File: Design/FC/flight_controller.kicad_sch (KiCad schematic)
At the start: 29 parts, among them U1 STM32H747BIT6, U3 BMI323, U4 MMC5983MA, U5 BMP390

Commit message: added flash memory
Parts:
- added C49: 100nF, symbol Device:C
- added FLASH_1: W25N01GWZEIG, Lib:W25N01GWZEIG, symbol W25N01GWZEIG:W25N01GWZEIG
- added R13, R14: 10K, symbol Device:R
- U1: footprint LQFP-208 -> Lib:STM32H747BIT6-LQFP-208
- U3: footprint BMI323_BOS -> Lib:BMI323_BOS
- U4: footprint MMC5983MA_MEM -> Lib:MMC5983MA_MEM
- U5: footprint BMP390-10LGA_2X2X0p75_BOS -> Lib:BMP390-10LGA_2X2X0p75_BOS
- renumbered BN880_Con to BN880_Con1, Debug_Con to Debug_Con1, Debug_UART to Debug_UART1, L_Motor to L_Motor1, RF_RECV_CONN to RF_RECV_CONN1, R_Motor to R_Motor1
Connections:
- net +3.3V: now also C49.1, FLASH_1.8 (VCC), R13.2, R14.1
- net GND: now also L_Servo_4.1 (Pin_1), U5.3 (VSS), C49.2, FLASH_1.4 (GND), FLASH_1.9 (EP)
- net FLASH_1_NSS: now reaches U1.166 (PA15)
- net FLASH_1_NSS: now also FLASH_1.1 (~{CS})
- net FLASH_1_SCK: now reaches U1.167 (PC10)
- net FLASH_1_SCK: now also FLASH_1.6 (CLK)
- net FLASH_1_MISO: now reaches U1.168 (PC11)
- net FLASH_1_MISO: now also FLASH_1.5 (DI_(IO0_))
- net FLASH_1_MOSI: now reaches U1.169 (PC12)
- net FLASH_1_MOSI: now also FLASH_1.2 (DO_(IO1_))
- net EXT_DEV_INT_BARO: no longer names the net of U1.66 (PI15)
- net I2C_1_SCL renamed CURRENT_SENSE_SCL
- net I2C_1_SDA renamed CURRENT_SENSE_SDA
- net TIM_4_CH_1: no longer names the net of U1.111 (PD12)
- new net: FLASH_1.3 (~{WP_(IO2_)}), R14.2
- new net: FLASH_1.7 (~{HOLD_(IO3_)}), R13.1
- no-connect marks 3 -> 111
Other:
- note added: "Current Sensor (Address: 0x40)"
- note added: "Flash Memory (1 Gbit)"
- moved on the sheet: C47, C48, RF_RECV_CONN1, U5

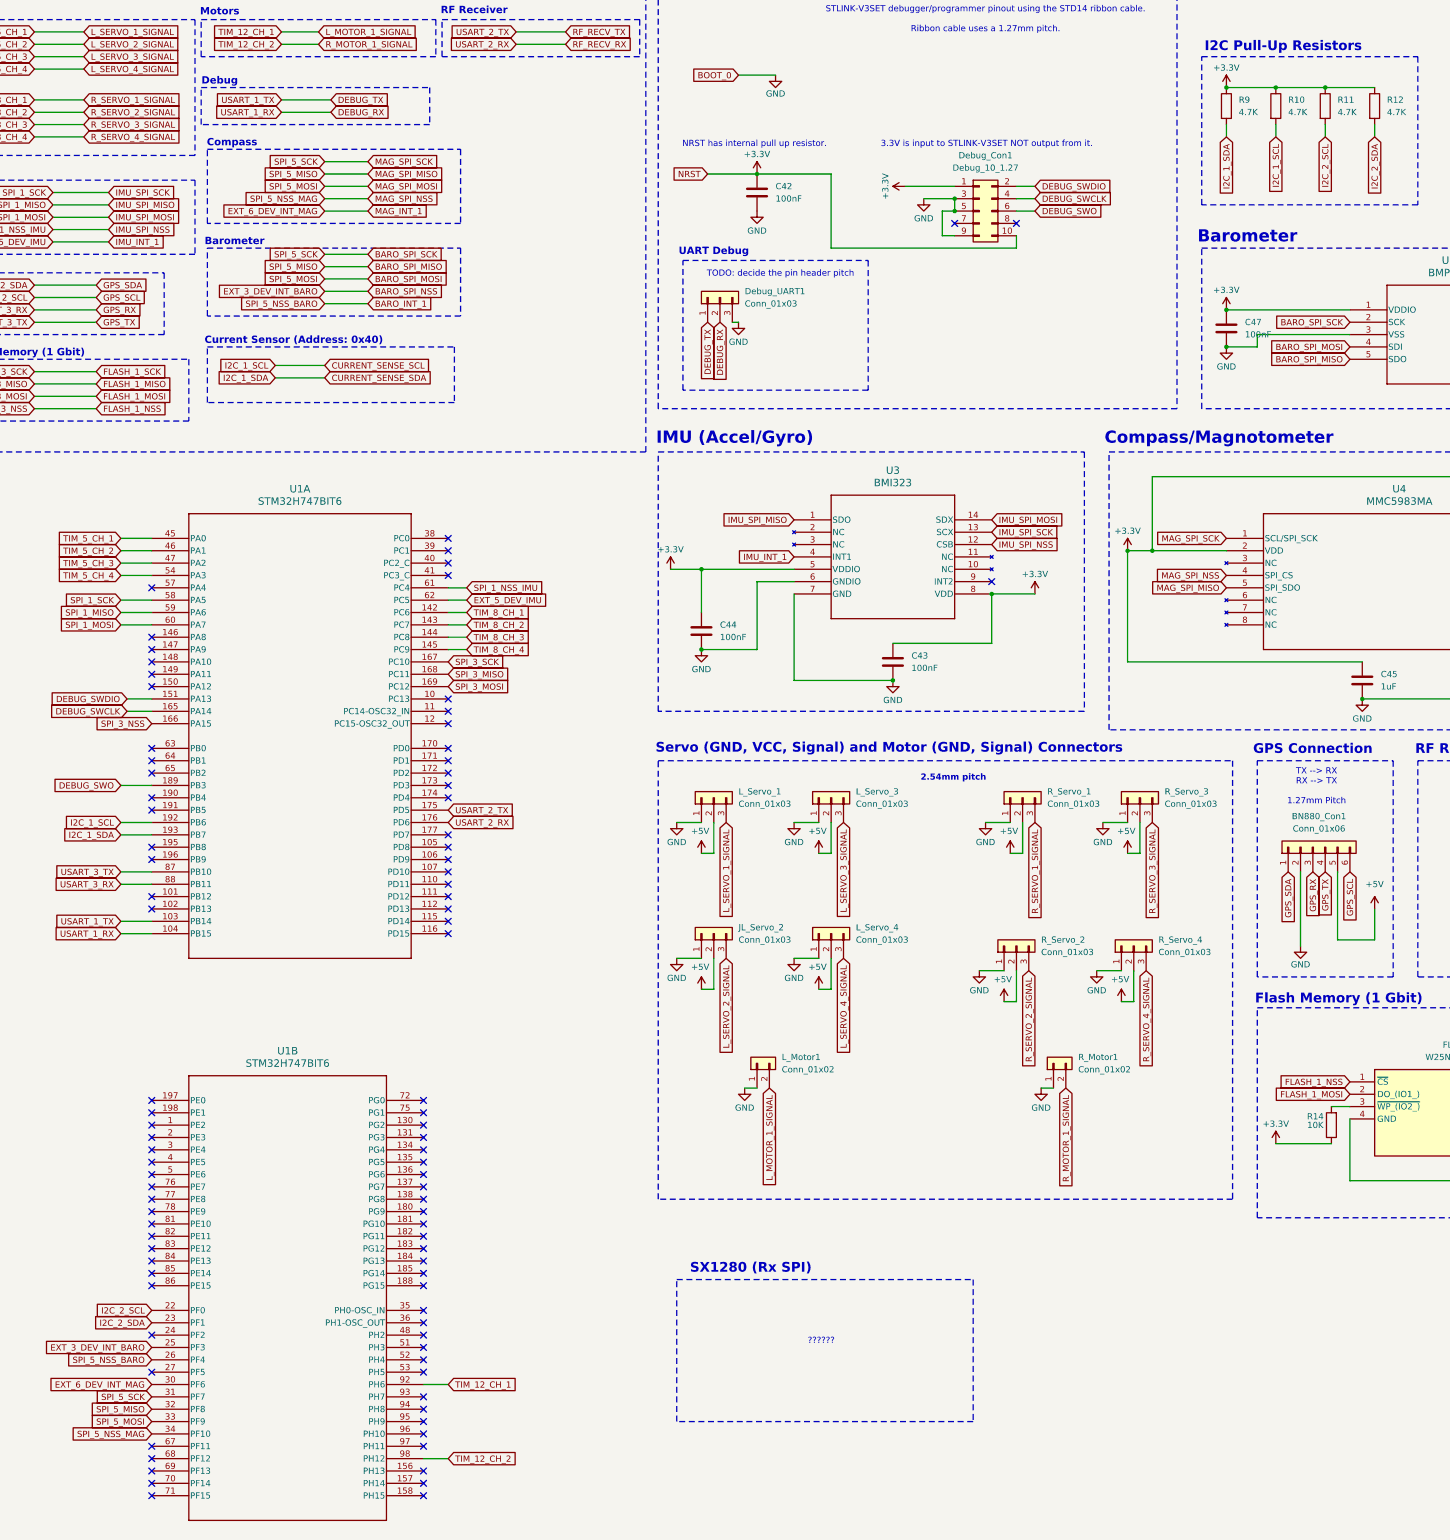
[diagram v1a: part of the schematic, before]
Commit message: started adding footprints and filling out bom
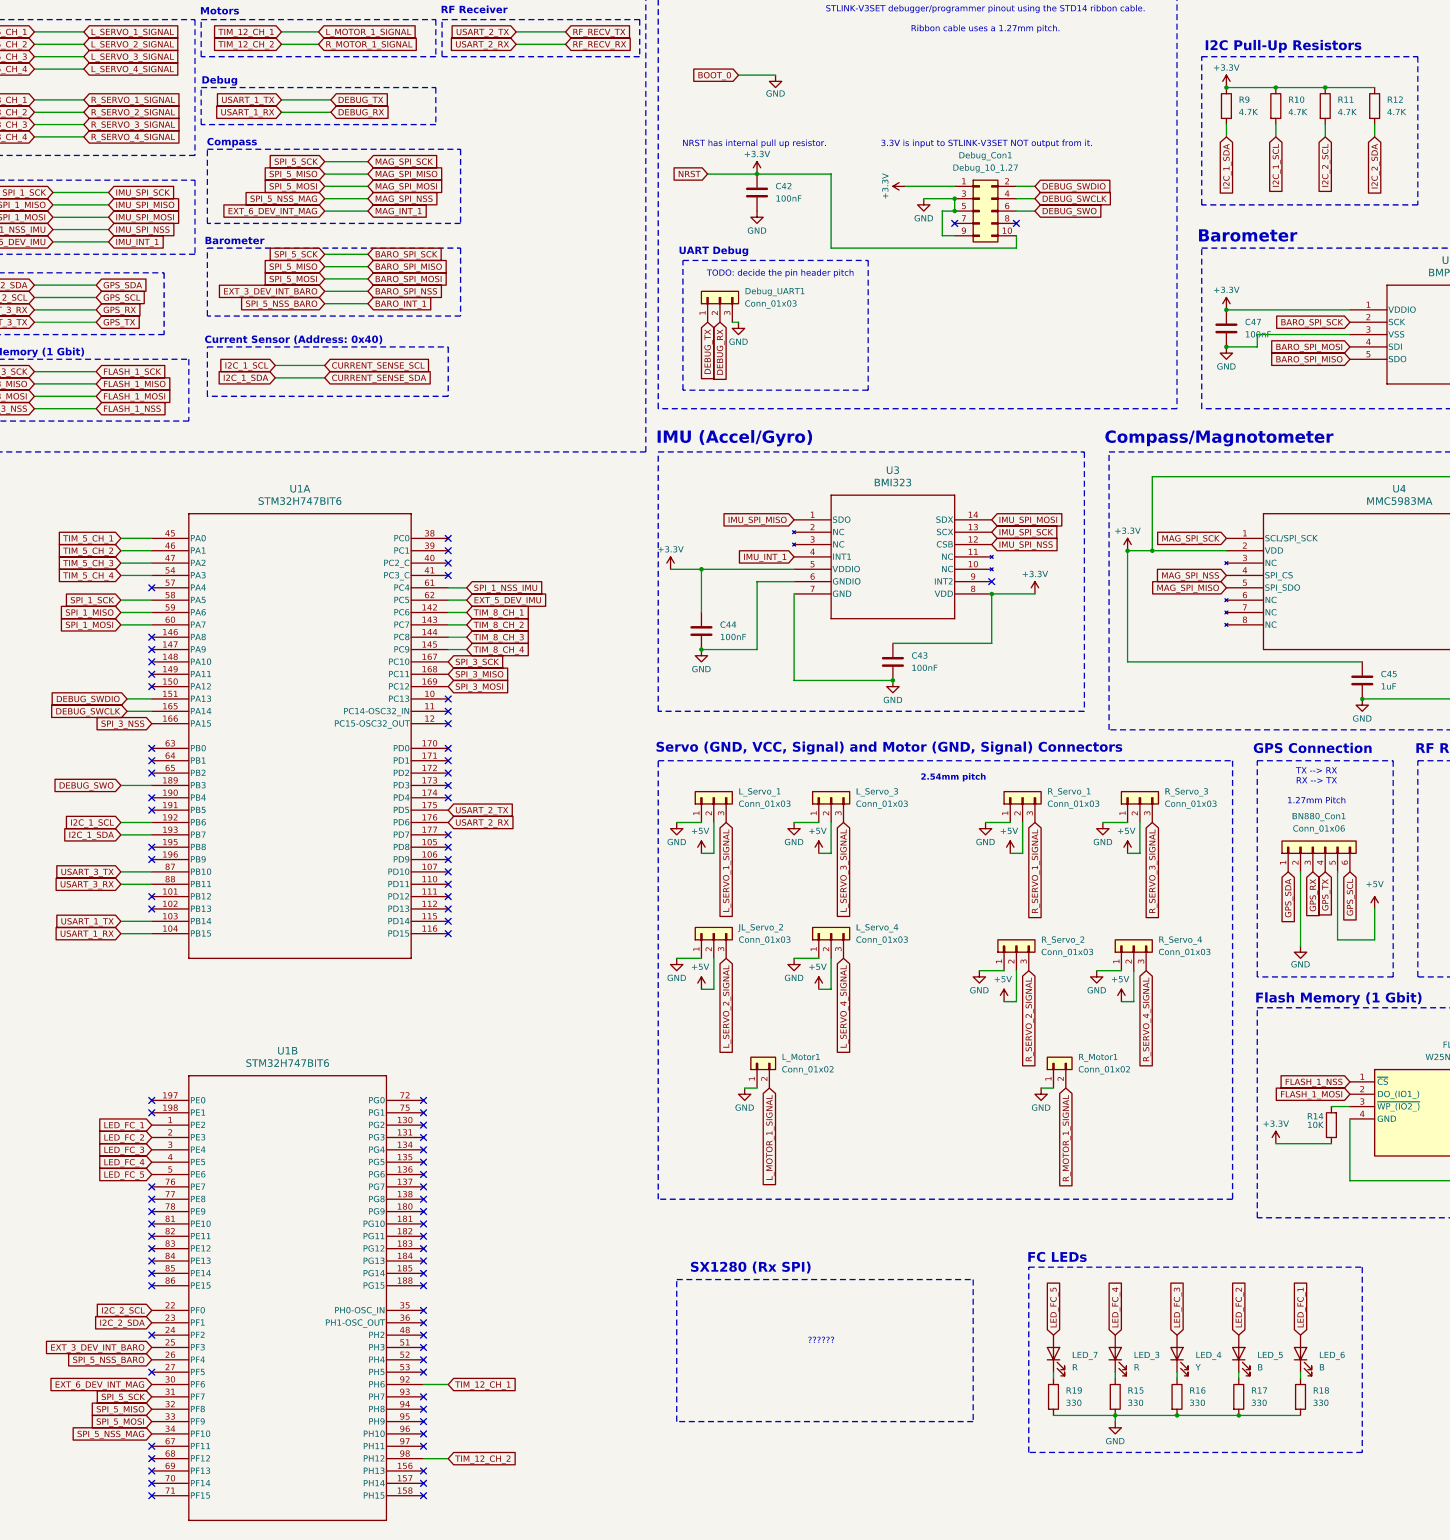
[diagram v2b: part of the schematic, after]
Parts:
- added LED_3, LED_7: R, symbol Device:LED
- added LED_4: Y, symbol Device:LED
- added LED_5, LED_6: B, symbol Device:LED
- added R15, R16, R17, R18, R19: 330, Resistor_SMD:R_0603_1608Metric_Pad0.98x0.95mm_HandSolder, symbol Device:R
- C42, C43, C44, C45, C46, C47, C48, C49: footprint (none) -> Capacitor_SMD:C_0603_1608Metric_Pad1.08x0.95mm_HandSolder
- Debug_Con1: footprint (none) -> Connector_PinHeader_1.27mm:PinHeader_2x05_P1.27mm_Vertical
- Debug_UART1, JL_Servo_2, L_Servo_1, L_Servo_3, L_Servo_4, R_Servo_1, R_Servo_2, R_Servo_3, R_Servo_4: footprint (none) -> Connector_PinHeader_2.54mm:PinHeader_1x03_P2.54mm_Vertical
- L_Motor1, R_Motor1: footprint (none) -> Connector_PinHeader_2.54mm:PinHeader_2x01_P2.54mm_Vertical
- R10, R11, R12, R13, R14, R9: footprint (none) -> Resistor_SMD:R_0603_1608Metric_Pad0.98x0.95mm_HandSolder
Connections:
- net GND: now also R15.2, R16.2, R17.2, R18.2, R19.2
- net LED_FC_1: now reaches U1.1 (PE2)
- net LED_FC_1: now also LED_6.2 (A)
- net LED_FC_2: now reaches U1.2 (PE3)
- net LED_FC_2: now also LED_5.2 (A)
- net LED_FC_3: now reaches U1.3 (PE4)
- net LED_FC_3: now also LED_4.2 (A)
- net LED_FC_4: now reaches U1.4 (PE5)
- net LED_FC_4: now also LED_3.2 (A)
- net LED_FC_5: now reaches U1.5 (PE6)
- net LED_FC_5: now also LED_7.2 (A)
- new net: LED_7.1 (K), R19.1
- new net: LED_3.1 (K), R15.1
- new net: LED_5.1 (K), R17.1
- new net: LED_4.1 (K), R16.1
- new net: LED_6.1 (K), R18.1
- no-connect marks 111 -> 106
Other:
- note added: "FC LEDs"

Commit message: started layout
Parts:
- added R21, R22, R23, R24, R25, R26, R27, R28, R29, R30, R31, R32, R33, R34, R35, R36, R37, R38, R39, R40, R41, R42, R43, R44, R45, R46, R47, R48, R49, R50, R51, R52, R53, R54, R55, R56, R57, R58, R61, R62, R64, R8: 0, symbol Device:R_Small_US
- BN880_Con1: footprint (none) -> Connector_PinHeader_1.27mm:PinHeader_1x06_P1.27mm_Horizontal
- LED_3, LED_4, LED_5, LED_6, LED_7: footprint (none) -> LED_SMD:LED_0603_1608Metric
- RF_RECV_CONN1: footprint (none) -> Connector_PinHeader_1.27mm:PinHeader_1x04_P1.27mm_Horizontal
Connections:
- net +3.3V: now also R61.1, R62.1, R64.2; no longer Debug_Con1.1 (Pin_1), Debug_Con1.10 (Pin_10), U1.37 (NRST)
- net BARO_INT_1: now also R43.2; no longer U1.26 (PF4)
- net BARO_SPI_MISO: now also R46.2; no longer U1.32 (PF8), U4.5 (SPI_SDO)
- net BARO_SPI_MOSI: now also R45.2; no longer U1.33 (PF9), U4.16 (SDA/SPI_SDI)
- net BARO_SPI_NSS: now also R44.2; no longer U1.25 (PF3)
- net BARO_SPI_SCK: now also R47.2; no longer U1.31 (PF7), U4.1 (SCL/SPI_SCK)
- net CURRENT_SENSE_SCL: now also R41.2; no longer R10.2, U1.192 (PB6)
- net CURRENT_SENSE_SDA: now also R42.2; no longer R9.2, U1.193 (PB7)
- net DEBUG_RX: now also R53.2; no longer U1.104 (PB15)
- net DEBUG_TX: now also R54.2; no longer U1.103 (PB14)
- net EXT_5_DEV_IMU: now also R32.1; no longer U3.4 (INT1)
- net EXT_6_DEV_INT_MAG: now also R48.1; no longer U4.15 (INT)
- net FLASH_1_MISO: now also R38.2; no longer U1.168 (PC11)
- net FLASH_1_MOSI: now also R39.2; no longer U1.169 (PC12)
- net FLASH_1_NSS: now also R40.2; no longer U1.166 (PA15)
- net FLASH_1_SCK: now also R37.2; no longer U1.167 (PC10)
- net GPS_RX: now also R35.2; no longer U1.88 (PB11)
- net GPS_SCL: now also R34.2; no longer R11.2, U1.22 (PF0)
- net GPS_SDA: now also R33.2; no longer R12.2, U1.23 (PF1)
- net GPS_TX: now also R36.2; no longer U1.87 (PB10)
- net IMU_SPI_MISO: now also R29.2; no longer U1.59 (PA6)
- net IMU_SPI_MOSI: now also R30.2; no longer U1.60 (PA7)
- net IMU_SPI_NSS: now also R31.2; no longer U1.61 (PC4)
- net IMU_SPI_SCK: now also R28.2; no longer U1.58 (PA5)
- net L_MOTOR_1_SIGNAL: now also R56.2; no longer U1.92 (PH6)
- net L_SERVO_1_SIGNAL: now also R21.2; no longer U1.45 (PA0)
- net L_SERVO_2_SIGNAL: now also R8.2; no longer U1.46 (PA1)
- net L_SERVO_3_SIGNAL: now also R22.2; no longer U1.47 (PA2)
- net L_SERVO_4_SIGNAL: now also R23.2; no longer U1.54 (PA3)
- net MAG_SPI_NSS: now also R49.2; no longer U1.34 (PF10)
- net RF_RECV_RX: now also R57.2; no longer U1.176 (PD6)
- net RF_RECV_TX: now also R58.2; no longer U1.175 (PD5)
- net R_MOTOR_1_SIGNAL: now also R55.2; no longer U1.98 (PH12)
- net R_SERVO_1_SIGNAL: now also R24.2; no longer U1.142 (PC6)
- net R_SERVO_2_SIGNAL: now also R25.2; no longer U1.143 (PC7), U1.205 (PI6)
- net R_SERVO_3_SIGNAL: now also R26.2; no longer U1.144 (PC8)
- net R_SERVO_4_SIGNAL: now also R27.2; no longer U1.145 (PC9)
- new net: Debug_Con1.1 (Pin_1), R61.2
- new net: Debug_Con1.10 (Pin_10), R62.2
- new net EXT_3_DEV_INT_BARO: R44.1, U1.25 (PF3)
- new net I2C_1_SCL: R10.2, R41.1, U1.192 (PB6)
- new net I2C_1_SDA: R42.1, R9.2, U1.193 (PB7)
- new net I2C_2_SCL: R11.2, R34.1, U1.22 (PF0)
- new net I2C_2_SDA: R12.2, R33.1, U1.23 (PF1)
- new net IMU_INT_1: R32.2, U3.4 (INT1)
- new net MAG_INT_1: R48.2, U4.15 (INT)
- new net MAG_SPI_MISO: R51.2, U4.5 (SPI_SDO)
- new net MAG_SPI_MOSI: R50.2, U4.16 (SDA/SPI_SDI)
- new net MAG_SPI_SCK: R52.2, U4.1 (SCL/SPI_SCK)
- new net NRST: R64.1, U1.37 (NRST)
- new net SPI_1_MISO: R29.1, U1.59 (PA6)
- new net SPI_1_MOSI: R30.1, U1.60 (PA7)
- new net SPI_1_NSS_IMU: R31.1, U1.61 (PC4)
- new net SPI_1_SCK: R28.1, U1.58 (PA5)
- new net SPI_3_MISO: R38.1, U1.168 (PC11)
- new net SPI_3_MOSI: R39.1, U1.169 (PC12)
- new net SPI_3_NSS: R40.1, U1.166 (PA15)
- new net SPI_3_SCK: R37.1, U1.167 (PC10)
- new net SPI_5_MISO: R46.1, R51.1, U1.32 (PF8)
- new net SPI_5_MOSI: R45.1, R50.1, U1.33 (PF9)
- new net SPI_5_NSS_BARO: R43.1, U1.26 (PF4)
- new net SPI_5_NSS_MAG: R49.1, U1.34 (PF10)
- new net SPI_5_SCK: R47.1, R52.1, U1.31 (PF7)
- new net TIM_12_CH_1: R56.1, U1.92 (PH6)
- new net TIM_12_CH_2: R55.1, U1.98 (PH12)
- new net TIM_5_CH_1: R21.1, U1.45 (PA0)
- new net TIM_5_CH_2: R8.1, U1.46 (PA1)
- new net TIM_5_CH_3: R22.1, U1.47 (PA2)
- new net TIM_5_CH_4: R23.1, U1.54 (PA3)
- new net TIM_8_CH_1: R24.1, U1.142 (PC6)
- new net TIM_8_CH_2: R25.1, U1.143 (PC7), U1.205 (PI6)
- new net TIM_8_CH_3: R26.1, U1.144 (PC8)
- new net TIM_8_CH_4: R27.1, U1.145 (PC9)
- new net USART_1_RX: R53.1, U1.104 (PB15)
- new net USART_1_TX: R54.1, U1.103 (PB14)
- new net USART_2_RX: R57.1, U1.176 (PD6)
- new net USART_2_TX: R58.1, U1.175 (PD5)
- new net USART_3_RX: R35.1, U1.88 (PB11)
- new net USART_3_TX: R36.1, U1.87 (PB10)

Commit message: started laying out voltage regulator
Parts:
- removed R21, R22, R23, R24, R25, R26, R27, R28, R29, R30, R31, R32, R33, R34, R35, R36, R37, R38, R39, R40, R41, R42, R43, R44, R45, R46, R47, R48, R49, R50, R51, R52, R53, R54, R55, R56, R57, R58, R61, R62, R8: 0, symbol Device:R_Small_US
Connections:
- net EXT_3_DEV_INT_BARO is gone; now on net BARO_SPI_NSS: U1.25 (PF3)
- net I2C_1_SCL is gone; now on net CURRENT_SENSE_SCL: R10.2, U1.192 (PB6)
- net I2C_1_SDA is gone; now on net CURRENT_SENSE_SDA: R9.2, U1.193 (PB7)
- net I2C_2_SCL is gone; now on net GPS_SCL: R11.2, U1.22 (PF0)
- net I2C_2_SDA is gone; now on net GPS_SDA: R12.2, U1.23 (PF1)
- net IMU_INT_1 is gone; now on net EXT_5_DEV_IMU: U3.4 (INT1)
- net MAG_INT_1 is gone; now on net EXT_6_DEV_INT_MAG: U4.15 (INT)
- net MAG_SPI_MISO is gone; now on net BARO_SPI_MISO: U4.5 (SPI_SDO)
- net MAG_SPI_MOSI is gone; now on net BARO_SPI_MOSI: U4.16 (SDA/SPI_SDI)
- net MAG_SPI_SCK is gone; now on net BARO_SPI_SCK: U4.1 (SCL/SPI_SCK)
- net SPI_1_MISO is gone; now on net IMU_SPI_MISO: U1.59 (PA6)
- net SPI_1_MOSI is gone; now on net IMU_SPI_MOSI: U1.60 (PA7)
- net SPI_1_NSS_IMU is gone; now on net IMU_SPI_NSS: U1.61 (PC4)
- net SPI_1_SCK is gone; now on net IMU_SPI_SCK: U1.58 (PA5)
- net SPI_3_MISO is gone; now on net FLASH_1_MISO: U1.168 (PC11)
- net SPI_3_MOSI is gone; now on net FLASH_1_MOSI: U1.169 (PC12)
- net SPI_3_NSS is gone; now on net FLASH_1_NSS: U1.166 (PA15)
- net SPI_3_SCK is gone; now on net FLASH_1_SCK: U1.167 (PC10)
- net SPI_5_MISO is gone; now on net BARO_SPI_MISO: U1.32 (PF8)
- net SPI_5_MOSI is gone; now on net BARO_SPI_MOSI: U1.33 (PF9)
- net SPI_5_NSS_BARO is gone; now on net BARO_INT_1: U1.26 (PF4)
- net SPI_5_NSS_MAG is gone; now on net MAG_SPI_NSS: U1.34 (PF10)
- net SPI_5_SCK is gone; now on net BARO_SPI_SCK: U1.31 (PF7)
- net TIM_12_CH_1 is gone; now on net L_MOTOR_1_SIGNAL: U1.92 (PH6)
- net TIM_12_CH_2 is gone; now on net R_MOTOR_1_SIGNAL: U1.98 (PH12)
- net TIM_5_CH_1 is gone; now on net L_SERVO_1_SIGNAL: U1.45 (PA0)
- net TIM_5_CH_2 is gone; now on net L_SERVO_2_SIGNAL: U1.46 (PA1)
- net TIM_5_CH_3 is gone; now on net L_SERVO_3_SIGNAL: U1.47 (PA2)
- net TIM_5_CH_4 is gone; now on net L_SERVO_4_SIGNAL: U1.54 (PA3)
- net TIM_8_CH_1 is gone; now on net R_SERVO_1_SIGNAL: U1.142 (PC6)
- net TIM_8_CH_2 is gone; now on net R_SERVO_2_SIGNAL: U1.143 (PC7), U1.205 (PI6)
- net TIM_8_CH_3 is gone; now on net R_SERVO_3_SIGNAL: U1.144 (PC8)
- net TIM_8_CH_4 is gone; now on net R_SERVO_4_SIGNAL: U1.145 (PC9)
- net USART_1_RX is gone; now on net DEBUG_RX: U1.104 (PB15)
- net USART_1_TX is gone; now on net DEBUG_TX: U1.103 (PB14)
- net USART_2_RX is gone; now on net RF_RECV_RX: U1.176 (PD6)
- net USART_2_TX is gone; now on net RF_RECV_TX: U1.175 (PD5)
- net USART_3_RX is gone; now on net GPS_RX: U1.88 (PB11)
- net USART_3_TX is gone; now on net GPS_TX: U1.87 (PB10)
- net +3.3V: now also Debug_Con1.1 (Pin_1); no longer C42.1
- net NRST: now also C42.1, Debug_Con1.10 (Pin_10)
